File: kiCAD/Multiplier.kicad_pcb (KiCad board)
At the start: 2 copper layers, 59 parts, among them IC2 ADG1221BRMZ, J1 Conn_01x02_Pin, J2 Conn_01x02_Pin, J3 Conn_01x02_Pin, Q7 Q_Dual_PNP_PNP_C1B1B2C2E2E1, Q8 Q_Dual_PNP_PNP_C1B1B2C2E2E1, U1 TS912, U10 TPS63060, U2 TLV340, U4 TS912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

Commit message: Modified: Multiplier.kicad_pcb, added: backups files
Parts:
- removed the R6 at (136.0, 141.3)
- added RV4: 3k, Potentiometer_SMD:Potentiometer_Bourns_3314G_Vertical, F.Cu at (104.6, 113.0)
- R22: value 3k -> 7,5k
- R3: value 25k -> 24k
- R6: value 10k -> 2k
- RV1: value 1,1k -> 1,15k
- RV2: value 12k -> 12,5k
- RV3: value 1,1k -> 2,4k
- moved J3 55.2 mm to (93.7, 132.3), turned to 180 degrees
- moved R6 47.8 mm to (110.9, 135.9), turned to 180 degrees
- moved R3 47.4 mm to (112.0, 151.9), turned to 90 degrees
- moved RV2 46.3 mm to (104.9, 150.1), turned to 180 degrees
- moved U2 42.9 mm to (111.4, 141.5)
- moved U7 41.2 mm to (111.4, 147.1)
- moved R14 35.0 mm to (96.8, 150.4), turned to -90 degrees
- moved R4 34.7 mm to (110.0, 151.9), turned to -90 degrees
- moved R13 33.8 mm to (94.7, 150.4), turned to 90 degrees
- moved RV3 32.9 mm to (90.4, 121.4), turned to 180 degrees
- moved U4 29.4 mm to (95.7, 145.4)
- moved R21 29.3 mm to (98.8, 114.3)
- moved R16 29.3 mm to (100.8, 128.0), turned to 180 degrees
- moved R23 28.5 mm to (95.0, 115.3), turned to 0 degrees
- moved R12 28.3 mm to (92.7, 150.4), turned to -90 degrees
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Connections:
- R22 pad 2: Net-(U5A--) -> Net-(R22-Pad2)
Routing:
- net VCC: track 0.00 -> 168.0 mm
- net Vcc-: track 0.00 -> 78.5 mm
- net Net-(U2B-+): track 0.00 -> 24.8 mm
- net Net-(U4A--): track 0.00 -> 23.2 mm
- net Net-(U7A-+): track 0.00 -> 22.5 mm
- net (UxUy + ErUy)/Asaw: track 0.00 -> 22.1 mm
- net Ux+Er: track 0.00 -> 21.4 mm
- net Net-(Q8B-C2): track 0.00 -> 20.8 mm
- net UyEr: track 0.00 -> 19.1 mm
- net PWM_OUT: track 0.00 -> 16.8 mm
- net Er: track 0.00 -> 16.4 mm
- net UxUy: track 0.00 -> 14.9 mm
- net Net-(R12-Pad2): track 0.00 -> 11.9 mm
- net Net-(U10-FB): track 0.00 -> 11.1 mm
- net VBUS: track 0.00 -> 11.0 mm
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
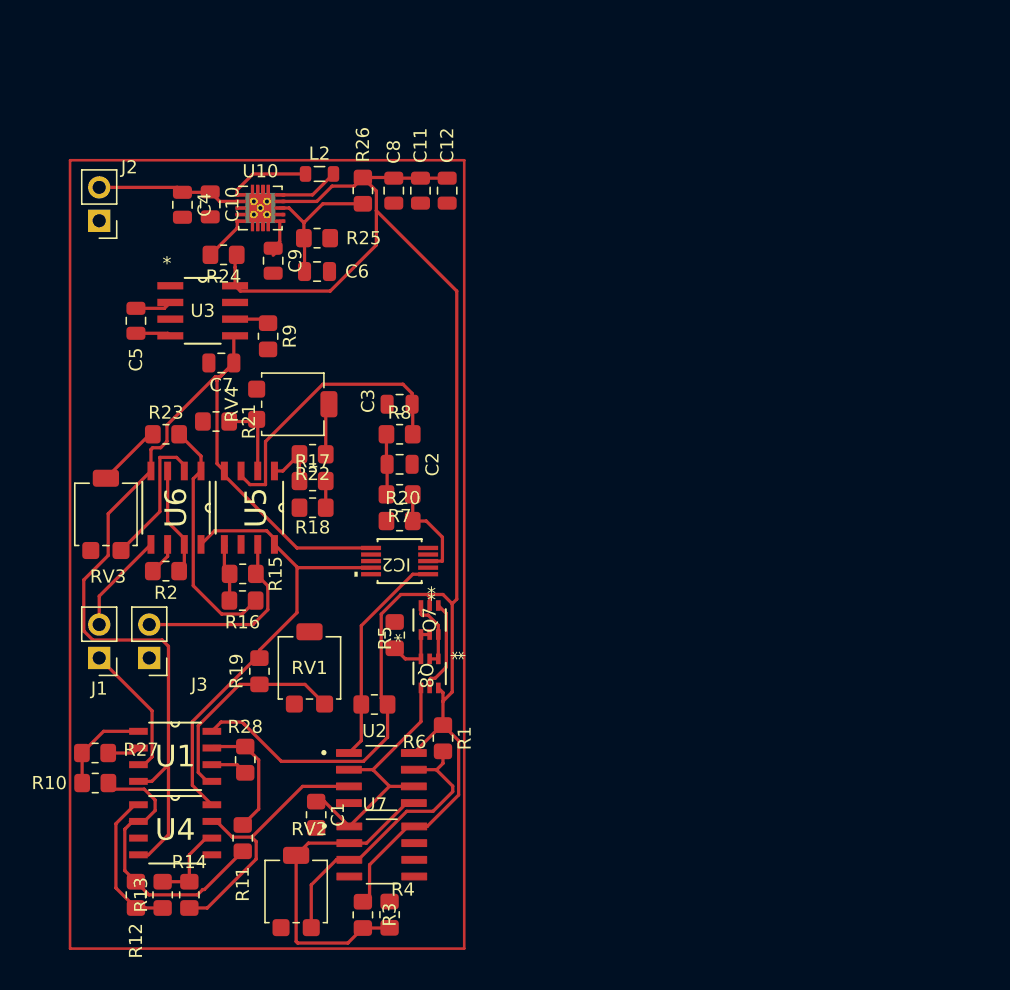
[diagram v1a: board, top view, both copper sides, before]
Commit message: Modified: Multiplier.kicad_pcb (fixed missing connections), added: backup files
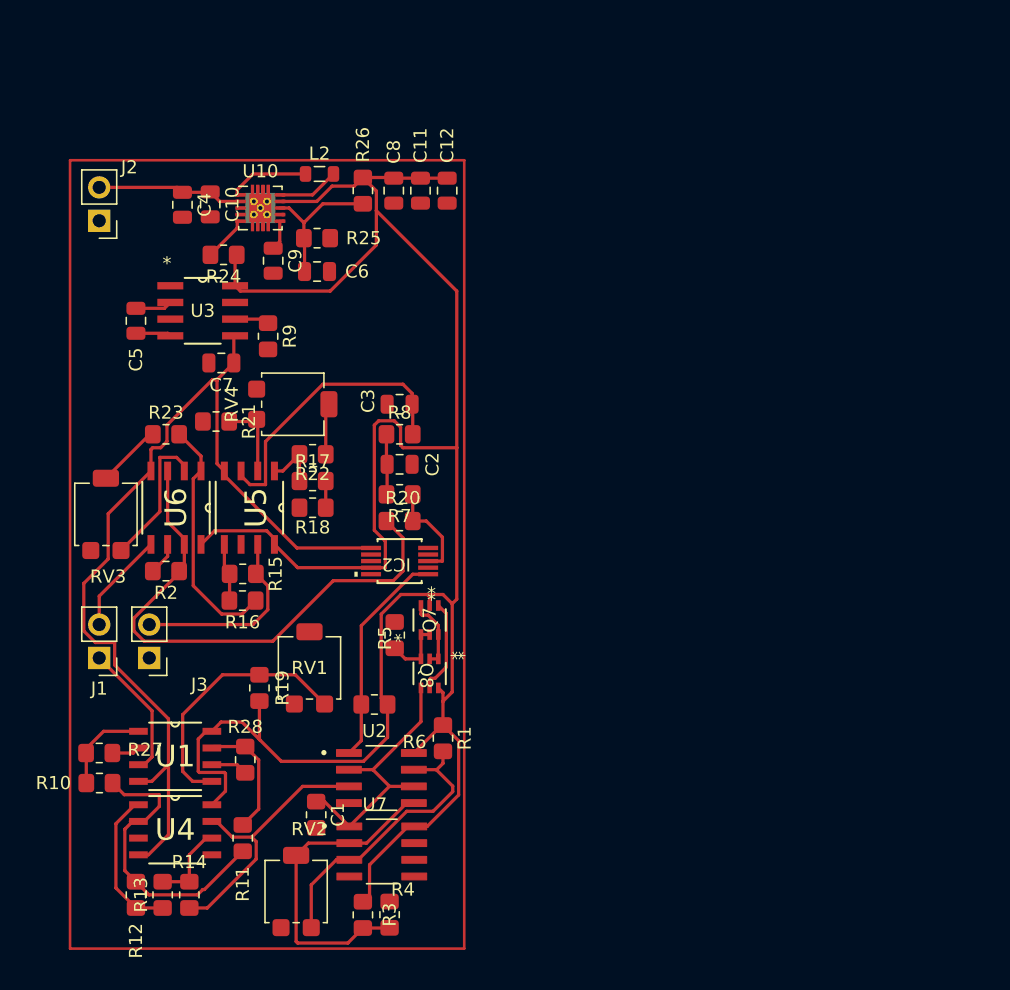
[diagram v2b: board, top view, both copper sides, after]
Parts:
- moved R19 1.27 mm to (102.1, 134.6), turned to 90 degrees
- moved R10 0.32 mm to (89.9, 141.9)
- moved R27 0.32 mm to (89.9, 139.6)
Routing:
- net Uy_buff: track 8.31 -> 40.5 mm
- net VCC: track 168.0 -> 175.4 mm
- net Vcc-: track 78.5 -> 73.1 mm
- net Er: track 16.4 -> 19.8 mm
- net Net-(U4A--): track 23.2 -> 22.1 mm
- net Net-(U4B--): track 6.86 -> 5.88 mm
- net Ux: track 10.9 -> 10.0 mm
- net Ux+Er: track 21.4 -> 20.6 mm
- net Net-(R12-Pad2): track 11.9 -> 11.1 mm
- net Net-(U5B-+): track 4.62 -> 3.86 mm
- net Net-(U10-VAUX): track 2.98 -> 2.27 mm
- net Net-(U7A-+): track 22.5 -> 21.8 mm
- net Net-(U1A--): track 2.82 -> 2.14 mm
- net Net-(U2B-+): track 24.8 -> 24.2 mm
- net VBUS: track 11.0 -> 10.4 mm
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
